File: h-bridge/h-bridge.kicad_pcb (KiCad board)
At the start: 2 copper layers, 65.5 x 50.5 mm, 29 parts, among them J1 Screw_Terminal_01x06, Q1 IRF4905, Q2 IRLZ44N, Q3 IRF4905, Q4 IRLZ44N, Q5 2N2222, Q6 2N2222, Q7 IRF4905, Q8 IRF4905

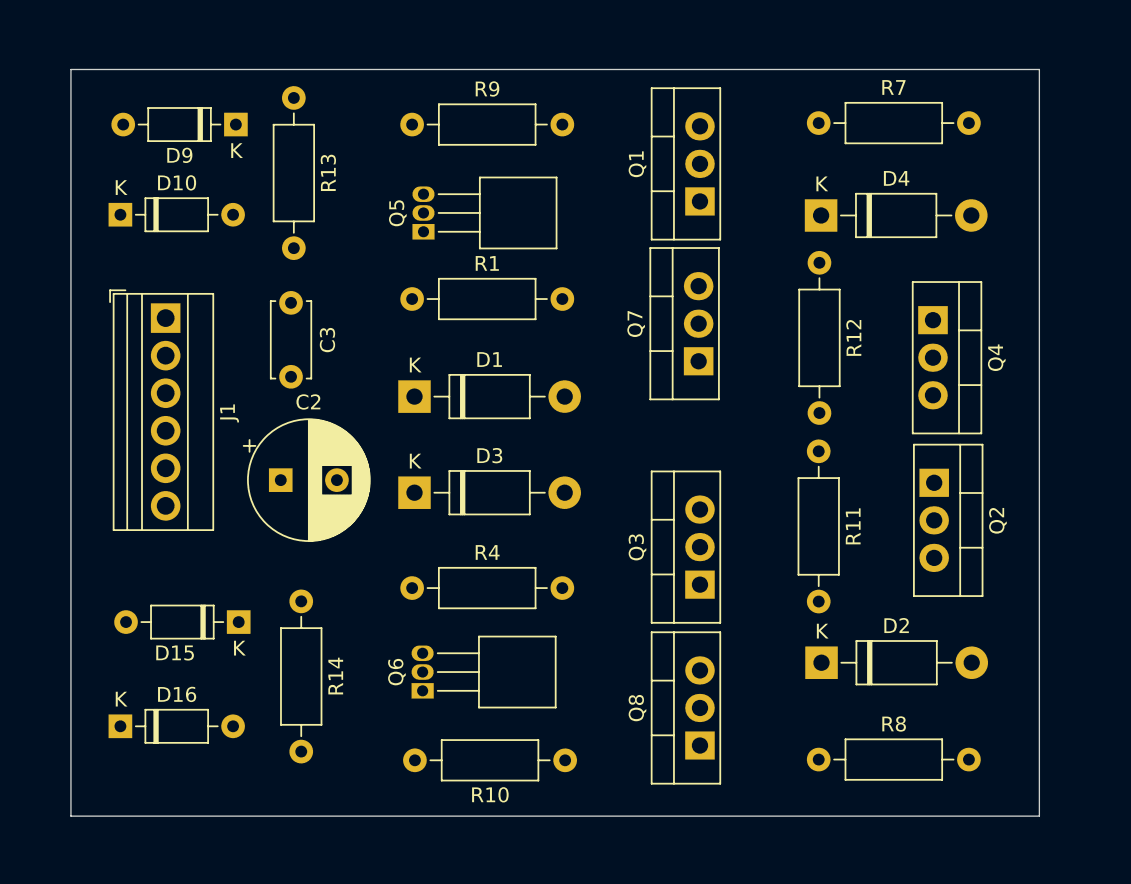
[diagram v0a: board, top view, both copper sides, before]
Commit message: pcb routed
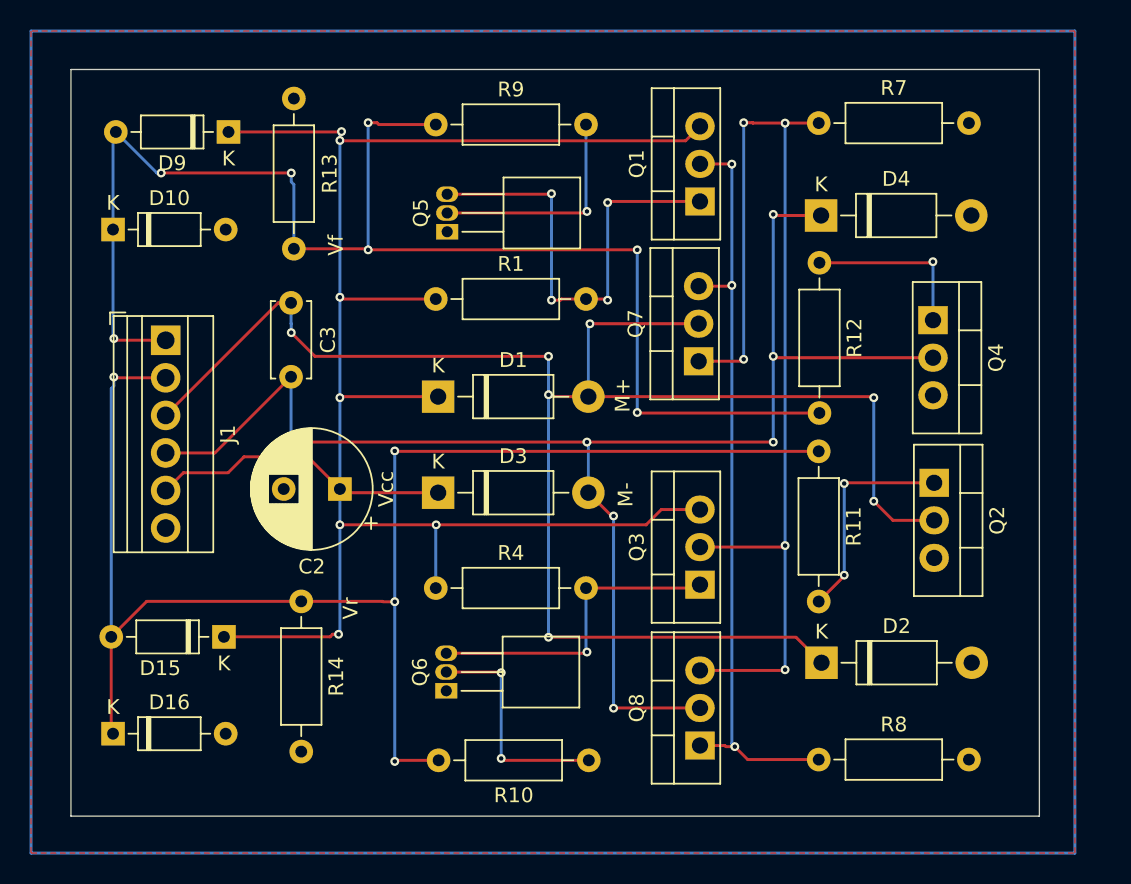
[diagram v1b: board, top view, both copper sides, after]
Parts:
- moved R13 10.2 mm to (110.6, 81.1), turned to 90 degrees
- moved C2 4.04 mm to (113.7, 97.4), turned to 180 degrees
- moved Q6 1.60 mm to (120.9, 111.0)
- moved D1 1.60 mm to (120.3, 91.1)
- moved D3 1.60 mm to (120.3, 97.6)
- moved Q5 1.60 mm to (120.9, 80.0)
- moved R1 1.60 mm to (120.2, 84.5)
- moved R10 1.60 mm to (130.5, 115.7)
- moved R4 1.60 mm to (120.2, 104.1)
- moved R9 1.60 mm to (120.2, 72.7)
- moved J1 1.50 mm to (101.9, 87.3)
- moved D15 1.41 mm to (105.8, 107.4)
- moved D10 1.12 mm to (98.3, 79.8)
- moved D16 0.71 mm to (98.3, 113.9)
- moved D9 0.71 mm to (106.2, 73.2)
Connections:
- C2 pad 2: Vcc -> GND
- D10 pad 2: Vcc -> GND
- D15 pad 1: VCC -> Vcc
- D16 pad 2: Vcc -> GND
- D2 pad 2: Vcc -> GND
- D4 pad 2: Vcc -> GND
- D9 pad 1: VCC -> Vcc
- J1 pad 6: Vcc -> GND
- Q2 pad 3: Vcc -> GND
- Q4 pad 3: Vcc -> GND
- Q5 pad 1: Vcc -> GND
- Q6 pad 1: Vcc -> GND
- R13 pad 2: Vcc -> GND
- R14 pad 2: Vcc -> GND
- R7 pad 2: Vcc -> GND
- R8 pad 2: Vcc -> GND
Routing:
- net Vcc: track 0.00 -> 137.0 mm, vias 0 -> 7
- net M+: track 0.00 -> 115.9 mm, vias 0 -> 7
- net M-: track 0.00 -> 101.8 mm, vias 0 -> 7
- net Vr: track 0.00 -> 100.6 mm, vias 0 -> 4
- net Vf: track 0.00 -> 95.7 mm, vias 0 -> 7
- net Net-(Q3-D): track 0.00 -> 72.7 mm, vias 0 -> 5
- net Net-(Q1-D): track 0.00 -> 52.3 mm, vias 0 -> 3
- net Net-(Q1-G): track 0.00 -> 31.0 mm, vias 0 -> 4
- net Net-(Q3-G): track 0.00 -> 21.7 mm, vias 0 -> 1
- net Net-(Q6-B): track 0.00 -> 15.5 mm, vias 0 -> 2
- net Net-(Q5-B): track 0.00 -> 15.4 mm, vias 0 -> 1
- net Net-(Q2-G): track 0.00 -> 14.8 mm, vias 0 -> 2
- net Net-(Q4-G): track 0.00 -> 11.7 mm, vias 0 -> 1
- added copper zone on B.Cu, net GND
- added copper zone on F.Cu, net GND
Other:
- board text added: "M+"
- board text added: "M-"
- board text added: "Vcc"
- board text added: "Vf"
- board text added: "Vr"

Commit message: gerber files done
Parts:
- renumbered C3 to C1, D9 to D1, D10 to D2, D15 to D3, D16 to D4, D1 to D5, D2 to D6, D3 to D7, D4 to D8, Q5 to Q1, Q1 to Q2, Q2 to Q3, Q7 to Q4, Q8 to Q5, Q3 to Q6, Q4 to Q7, Q6 to Q8, R13 to R1, R14 to R2, R9 to R3, R1 to R4, R11 to R5, R7 to R6, R8 to R7, R12 to R8, R4 to R9
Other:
- board size 65.5 x 50.5 mm -> 66.1 x 50.5 mm
- board text added: "IN1|IN2|M1|M2|PWR|GND"

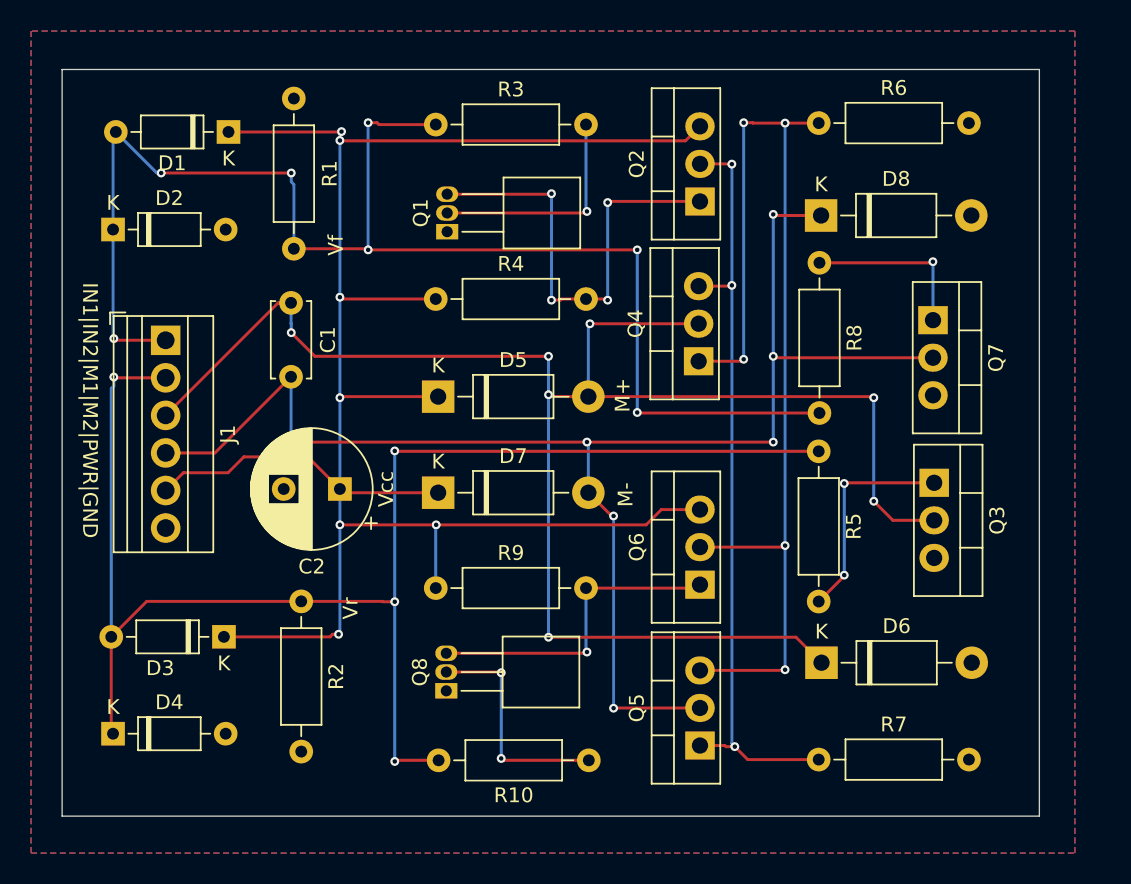
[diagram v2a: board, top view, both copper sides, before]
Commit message: V2 Redesign Submitted to JLCPCB and BOM generated
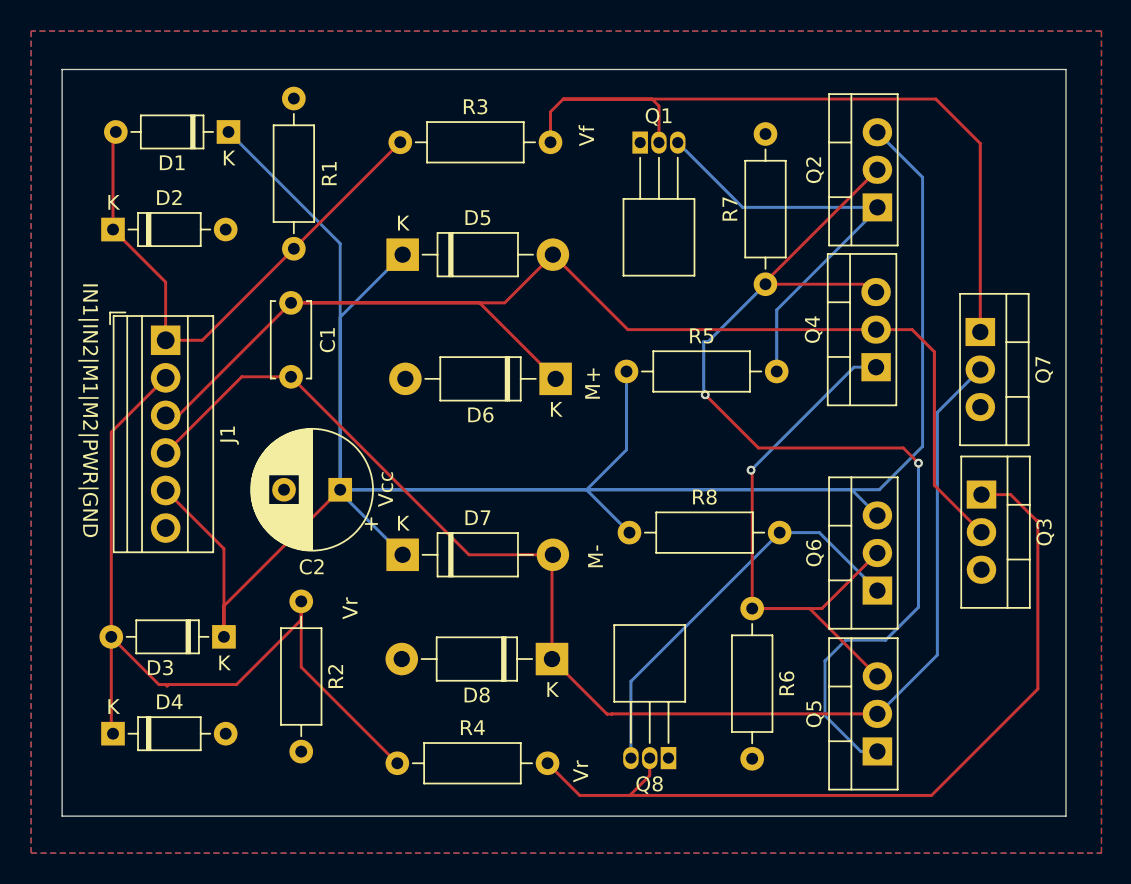
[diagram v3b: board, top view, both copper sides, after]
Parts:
- removed R10: 470, Resistor_THT:R_Axial_DIN0207_L6.3mm_D2.5mm_P10.16mm_Horizontal
- removed R9: 1k, Resistor_THT:R_Axial_DIN0207_L6.3mm_D2.5mm_P10.16mm_Horizontal
- R4: value 1k -> 470
- R5, R8: value 470 -> 1k
- moved D8 35.1 mm to (128.0, 108.9), turned to 180 degrees
- moved R6 33.1 mm to (141.6, 105.5), turned to -90 degrees
- moved R7 32.4 mm to (142.5, 83.5), turned to 90 degrees
- moved R4 31.5 mm to (117.6, 115.9)
- moved D6 26.3 mm to (128.3, 89.9), turned to 180 degrees
- moved R8 22.3 mm to (133.3, 100.3), turned to 0 degrees
- moved Q8 15.7 mm to (135.9, 115.6), turned to 180 degrees
- moved Q1 14.4 mm to (134.0, 73.9), turned to 0 degrees
- moved R5 14.1 mm to (133.1, 89.4), turned to 0 degrees
- moved Q2 12.0 mm to (150.0, 78.3)
- moved Q4 12.0 mm to (150.0, 89.1)
- moved Q5 12.0 mm to (150.0, 115.1)
- moved Q6 12.0 mm to (150.0, 104.2)
- moved D5 9.90 mm to (117.9, 81.5)
- moved D7 4.84 mm to (117.9, 101.8)
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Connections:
- D1 pad 2: Vf -> Net-(D1-A)
- D2 pad 1: Vf -> Net-(D1-A)
- D3 pad 2: Vr -> Net-(D3-A)
- D4 pad 1: Vr -> Net-(D3-A)
- J1 pad 1: Vf -> Net-(D1-A)
- J1 pad 2: Vr -> Net-(D3-A)
- Q1 pad 2: Net-(Q1-B) -> Vf
- Q3 pad 1: Net-(Q3-G) -> Vr
- Q7 pad 1: Net-(Q7-G) -> Vf
- Q8 pad 2: Net-(Q8-B) -> Vr
- R1 pad 1: Vf -> Net-(D1-A)
- R2 pad 1: Vr -> Net-(D3-A)
- R3 pad 1: Vf -> Net-(D1-A)
- R3 pad 2: Net-(Q1-B) -> Vf
- R4 pad 1: Vcc -> Net-(D3-A)
- R4 pad 2: Net-(Q1-C) -> Vr
- R5 pad 1: Vr -> Vcc
- R5 pad 2: Net-(Q3-G) -> Net-(Q1-C)
- R8 pad 1: Net-(Q7-G) -> Vcc
- R8 pad 2: Vf -> Net-(Q6-G)
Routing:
- net Vcc: track 137.0 -> 205.9 mm, vias 7 -> 0
- net Net-(D3-A): track 0.00 -> 56.6 mm
- net Vr: track 100.6 -> 56.1 mm, vias 4 -> 0
- net Vf: track 95.7 -> 54.6 mm, vias 7 -> 0
- net Net-(D1-A): track 0.00 -> 37.1 mm
- net Net-(Q4-G): track 72.7 -> 41.1 mm, vias 5 -> 1
- net M+: track 115.9 -> 92.8 mm, vias 7 -> 0
- net Net-(Q2-D): track 52.3 -> 70.2 mm, vias 3 -> 2
- net Net-(Q8-B): track 15.5 -> 0.00 mm, vias 2 -> 0
- net Net-(Q1-B): track 15.4 -> 0.00 mm, vias 1 -> 0
- net Net-(Q3-G): track 14.8 -> 0.00 mm, vias 2 -> 0
- net Net-(Q7-G): track 11.7 -> 0.00 mm, vias 1 -> 0
- net M-: track 101.8 -> 90.2 mm, vias 7 -> 0
- net Net-(Q6-G): track 21.7 -> 27.7 mm, vias 1 -> 0
- net Net-(Q1-C): track 31.0 -> 29.2 mm, vias 4 -> 0
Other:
- board size 66.1 x 50.5 mm -> 67.9 x 50.5 mm

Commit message: V3 submitted to JLCPCB
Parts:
- Q1, Q8: footprint Package_TO_SOT_THT:TO-92_Inline_Horizontal1 -> Package_TO_SOT_THT:TO-92_HandSolder
- Q2, Q4, Q5, Q6: value IRF4905 -> FQP27P06
- moved R5 10.5 mm to (143.6, 89.2), turned to 180 degrees
- moved R8 10.3 mm to (143.5, 100.2), turned to 180 degrees
- moved Q8 4.70 mm to (136.1, 110.9)
- moved Q1 4.02 mm to (133.6, 77.9)
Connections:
- D1 pad 2: Net-(D1-A) -> Vf
- D2 pad 1: Net-(D1-A) -> Vf
- D3 pad 2: Net-(D3-A) -> Vr
- D4 pad 1: Net-(D3-A) -> Vr
- J1 pad 1: Net-(D1-A) -> Vf
- J1 pad 2: Net-(D3-A) -> Vr
- Q1 pad 2: Vf -> Net-(Q1-B)
- Q8 pad 2: Vr -> Net-(Q8-B)
- R1 pad 1: Net-(D1-A) -> Vf
- R2 pad 1: Net-(D3-A) -> Vr
- R3 pad 1: Net-(D1-A) -> Vf
- R3 pad 2: Vf -> Net-(Q1-B)
- R4 pad 1: Net-(D3-A) -> Net-(Q8-B)
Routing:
- net Vr: track 56.1 -> 115.4 mm
- net Vcc: track 205.9 -> 146.8 mm
- net Net-(D3-A): track 56.6 -> 0.00 mm
- net Net-(D1-A): track 37.1 -> 0.00 mm
- net Vf: track 54.6 -> 89.9 mm
- net Net-(Q8-B): track 0.00 -> 21.3 mm
- net M+: track 92.8 -> 81.0 mm
- net M-: track 90.2 -> 101.4 mm
- net Net-(Q4-G): track 41.1 -> 50.8 mm, vias 1 -> 0
- net Net-(Q1-B): track 0.00 -> 8.07 mm
- net Net-(Q2-D): track 70.2 -> 64.7 mm, vias 2 -> 0
- net Net-(Q6-G): track 27.7 -> 32.7 mm
- net Net-(Q1-C): track 29.2 -> 26.5 mm
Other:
- outline, holes or cut-outs redrawn
